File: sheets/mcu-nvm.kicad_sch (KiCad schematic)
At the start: 49 parts

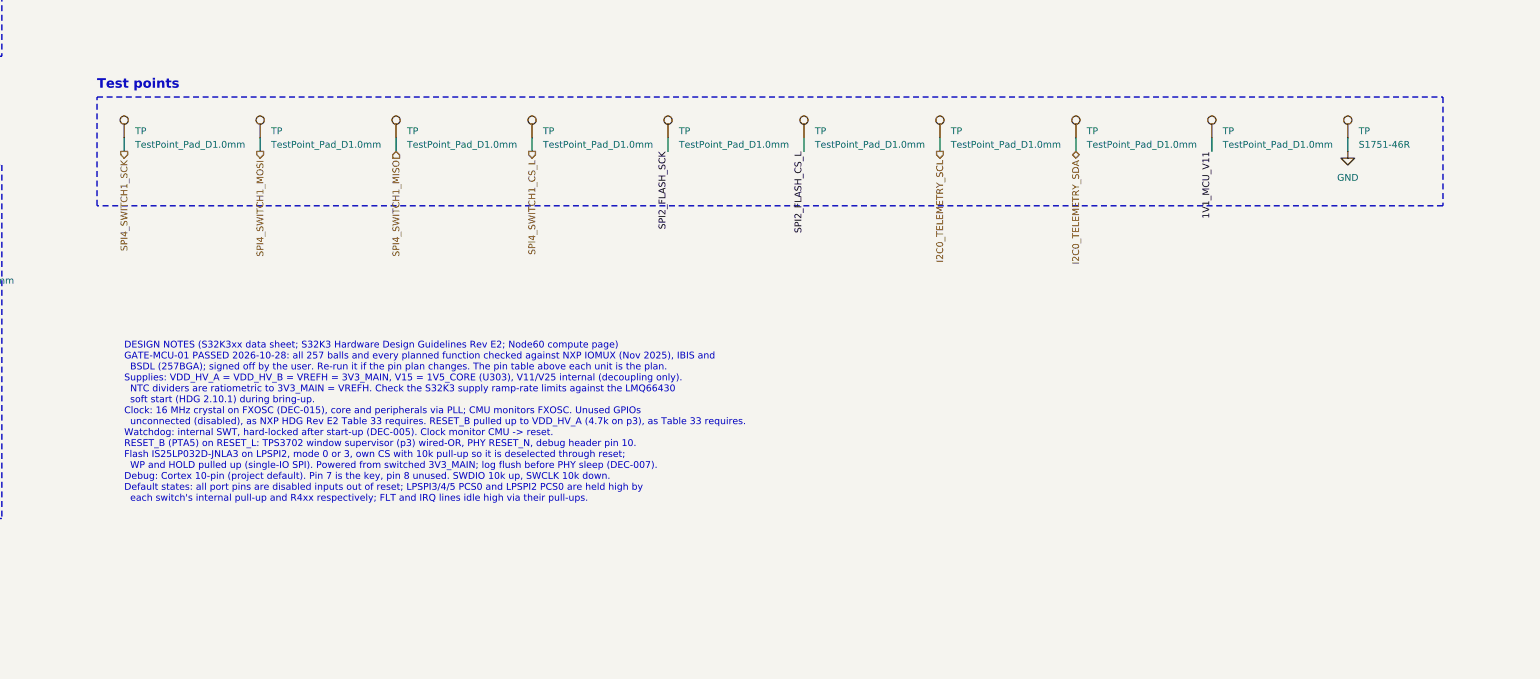
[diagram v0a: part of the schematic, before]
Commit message: GATE-MCU-01 re-run passed; test points on every SPI5 and SPI3 line
- The user signed off GATE-MCU-01 for DEC-018's eight added balls (2026-10-30);
  gate status back to passed on the gates list, gate page, DEC-018, compute and
  revisions pages, CLAUDE.md and the p4 design notes.
- TP413-TP416 (SPI5_SWITCH2_SCK/MOSI/MISO/CS_L) and TP417-TP420 (SPI3_SWITCH3_*)
  added as a second row in the p4 Test points box; box grown and the design
  notes moved down to fit. Netlist checked; ERC unchanged.

Co-Authored-By: Claude Opus 5.5 <noreply@anthropic.com>
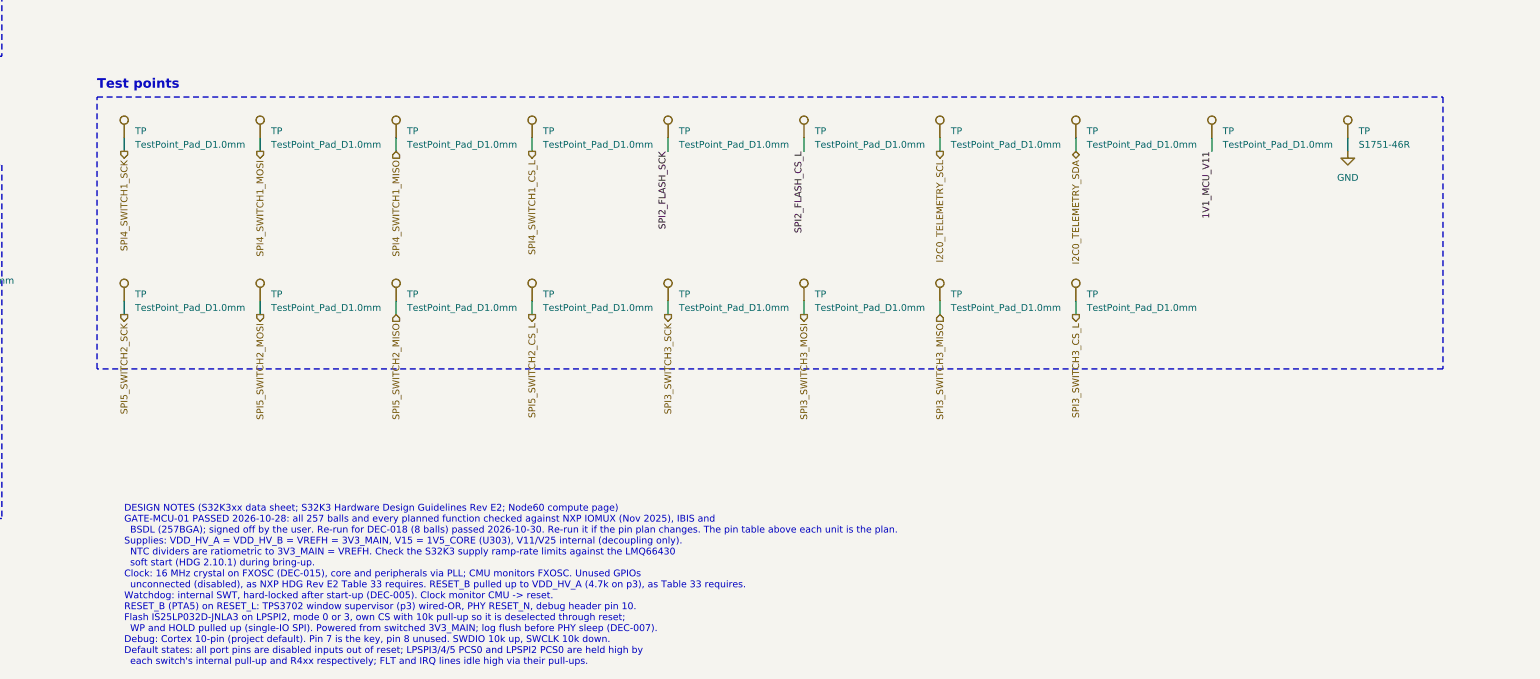
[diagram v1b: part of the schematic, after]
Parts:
- added TP (x8): TestPoint_Pad_D1.0mm, DropOut_TestPoint:TestPoint_Pad_D1.0mm, symbol DropOut_Connector:TestPoint_Pad_D1.0mm
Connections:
- net SPI3_SWITCH3_CS_L: now also TP.1
- net SPI3_SWITCH3_MISO: now also TP.1
- net SPI3_SWITCH3_MOSI: now also TP.1
- net SPI3_SWITCH3_SCK: now also TP.1
- net SPI5_SWITCH2_CS_L: now also TP.1
- net SPI5_SWITCH2_MISO: now also TP.1
- net SPI5_SWITCH2_MOSI: now also TP.1
- net SPI5_SWITCH2_SCK: now also TP.1
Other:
- note added: "DESIGN NOTES (S32K3xx data sheet; S32K3 Hardware Design Guidelines Rev E2; Node60 compute page) GATE-MCU-01 PASSED 2026-10-28: all 257 balls and every planned function checked against NXP IOMUX (Nov 2025), IBIS and BSDL (257BGA); signed off by the user. Re-run for DEC-018 (8 balls) passed 2026-10-30. Re-run it if the pin plan changes. The pin table above each unit is the plan. Supplies: VDD_HV_A 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"
- note removed: "DESIGN NOTES (S32K3xx data sheet; S32K3 Hardware Design Guidelines Rev E2; Node60 compute page) GATE-MCU-01 PASSED 2026-10-28: all 257 balls and every planned function checked against NXP IOMUX (Nov 2025), IBIS and BSDL (257BGA); signed off by the user. Re-run it if the pin plan changes. The pin table above each unit is the plan. Supplies: VDD_HV_A = VDD_HV_B = VREFH = 3V3_MAIN, V15 = 1V5_CORE (U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"
